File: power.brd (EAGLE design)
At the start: 95.2 x 82.5 mm, 60 parts, among them IC1 7812DT, IC2 7805TV, IC3 78L05F, U1 P82B96D, U2 P82B96D

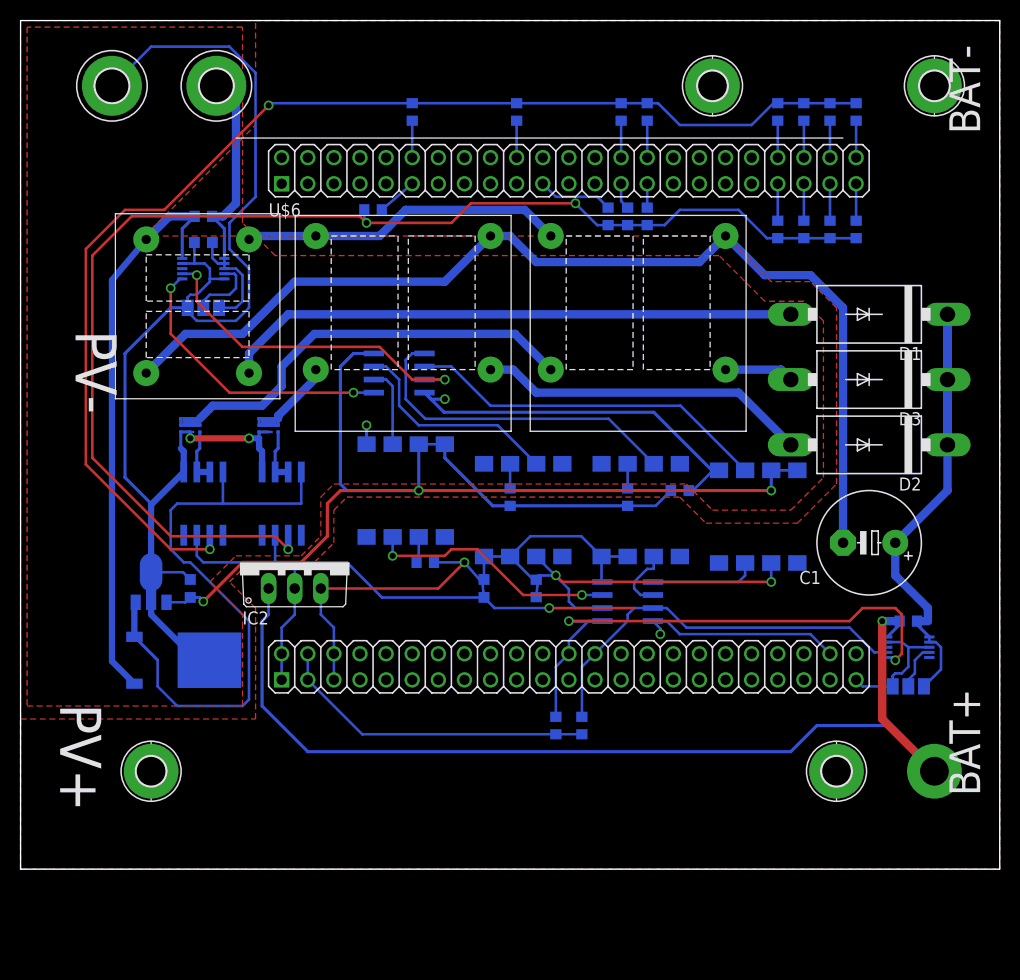
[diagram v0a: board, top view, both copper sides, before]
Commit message: sending out for another prototype
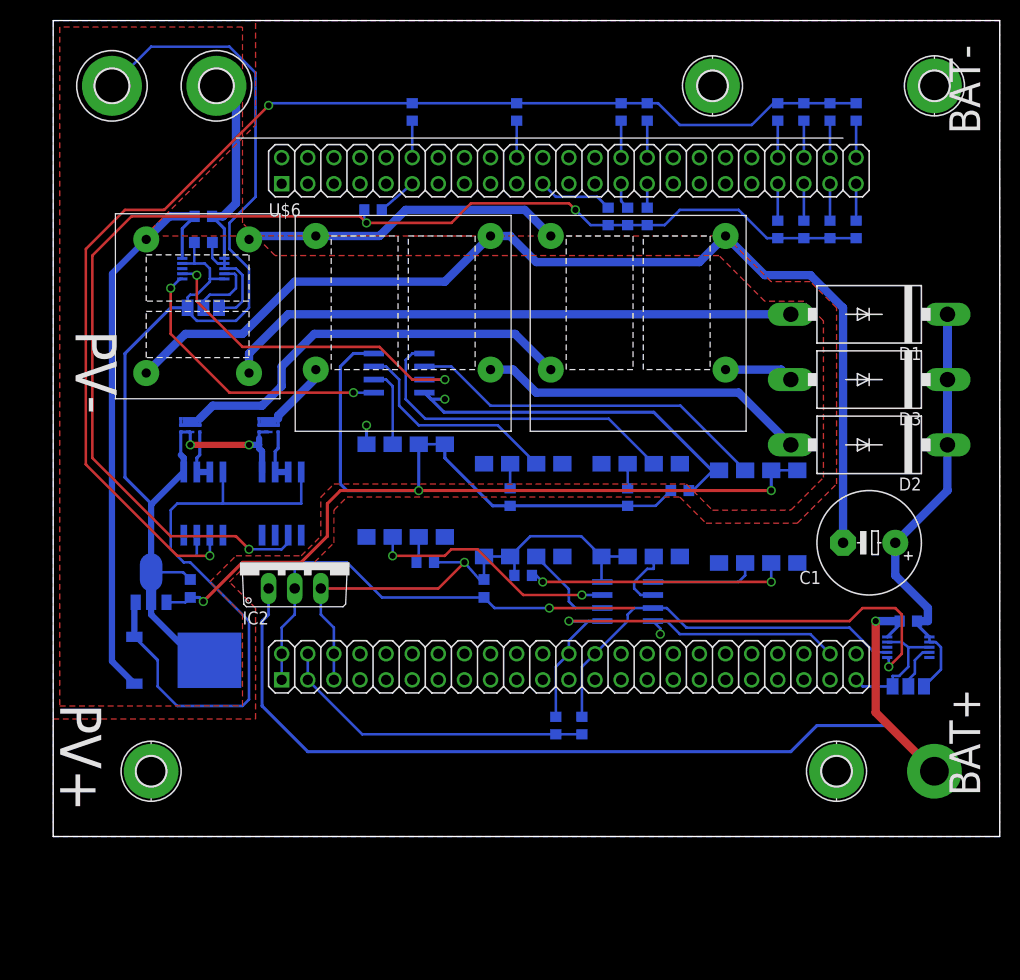
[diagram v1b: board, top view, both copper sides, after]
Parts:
- moved R5 1.80 mm to (42.5, 22.2), turned to 180 degrees
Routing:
- net GND: track 197.6 -> 183.0 mm
- net N$7: track 26.9 -> 25.4 mm
- net VCC: track 54.1 -> 52.6 mm
- net SCL: track 54.0 -> 55.0 mm
- net N$45: track 120.4 -> 121.3 mm
- net N$4: track 102.3 -> 103.2 mm
- net PGND: track 167.2 -> 167.8 mm
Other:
- board size 95.2 x 82.5 mm -> 92.1 x 79.4 mm

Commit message: fixed labels
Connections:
- removed net N$17: U$6.77
- removed net N$18: U$6.76
- removed net N$19: U$6.75
- removed net N$20: U$6.87
- removed net N$22: U$6.74
- removed net N$23: U$6.73
- removed net N$24: U$6.71

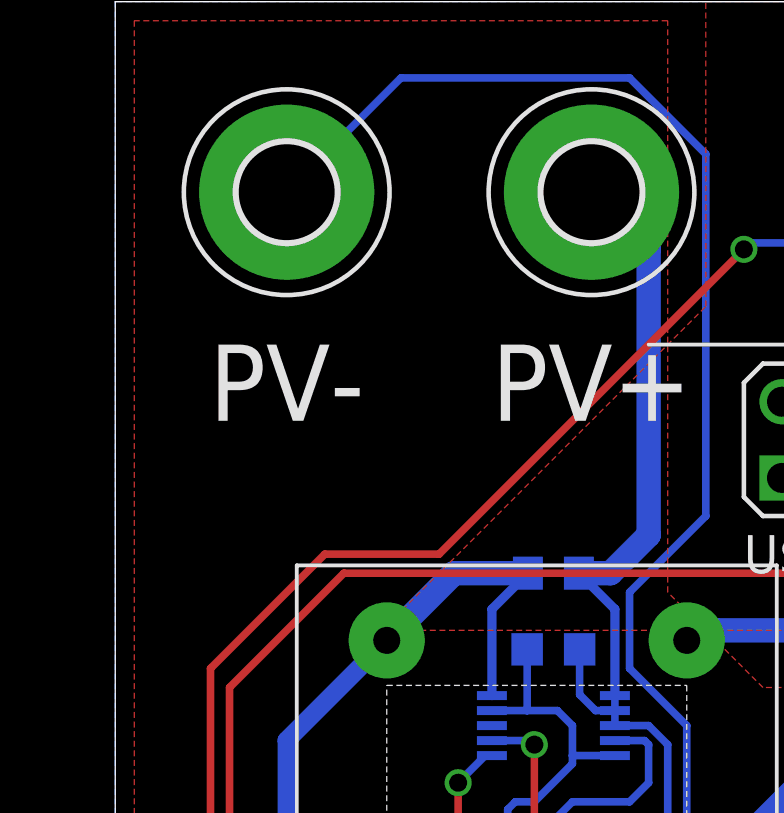
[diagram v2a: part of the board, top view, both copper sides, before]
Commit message: input capacitor? might help.
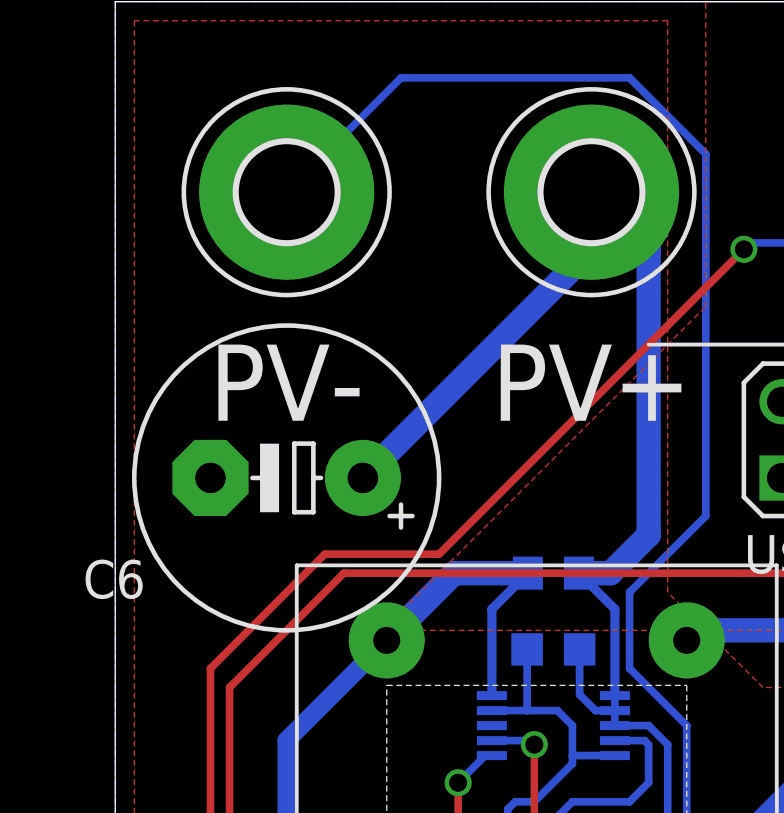
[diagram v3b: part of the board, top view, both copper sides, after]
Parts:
- added C6: 100u, rcl:E5-10,5
- C1: value (none) -> 100u
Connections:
- net PGND: now also C6.-
- net PV: now also C6.+
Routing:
- net PV: track 30.7 -> 43.3 mm
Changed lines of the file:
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@@
 <element name="D2" library="diode" package="DO201-15" value="BY500" x="76.2" y="34.925" rot="R180"/>
 <element name="D3" library="diode" package="DO201-15" value="BY500" x="76.2" y="41.275" rot="R180"/>
-<element name="C1" library="rcl" package="E5-10,5" value="" x="76.2" y="25.4" rot="R180"/>
+<element name="C1" library="rcl" package="E5-10,5" value="100u" x="76.2" y="25.4" rot="R180"/>
 <element name="R1" library="rcl" package="R0603" value="0R2" x="80.01" y="17.78" rot="MR0"/>
 <element name="R2" library="rcl" package="R0603" value="0R2" x="11.43" y="57.15" rot="MR0"/>
@@
 <element name="C4" library="rcl" package="C0603K" value="0.1u" x="57.785" y="30.48" rot="MR180"/>
 <element name="C5" library="rcl" package="C0603K" value="0.1u" x="38.735" y="20.955" rot="MR270"/>
+<element name="C6" library="rcl" package="E5-10,5" value="100u" x="2.54" y="60.325" rot="R180"/>
 </elements>
 <signals>
@@
 <wire x1="14.605" y1="58.42" x2="13.335" y2="57.15" width="0.8128" layer="16"/>
 <wire x1="13.335" y1="57.15" x2="12.28" y2="57.15" width="0.8128" layer="16"/>
+<contactref element="C6" pad="+"/>
+<wire x1="5.08" y1="60.325" x2="12.7" y2="67.945" width="0.8128" layer="16"/>
+<wire x1="12.7" y1="67.945" x2="12.7" y2="69.85" width="0.8128" layer="16"/>
 </signal>
 <signal name="N$10">
@@
 <wire x1="12.065" y1="51.07" x2="12.065" y2="50.8" width="0.254" layer="16"/>
 <wire x1="15.875" y1="34.925" x2="16.855" y2="34.925" width="0.6096" layer="16"/>
+<contactref element="C6" pad="-"/>
 </signal>
 <signal name="N$8">

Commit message: important fixes... and that 7812 that isn't actually a 7812 is still a problem
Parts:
- moved C4 33.3 mm to (25.4, 38.1)
- moved R31 6.54 mm to (49.5, 35.6), turned to 0 degrees
- moved R32 5.68 mm to (38.7, 34.9), turned to 0 degrees
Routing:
- net N$43: track 126.0 -> 105.7 mm, vias 3 -> 4
- net N$49: track 2.39 -> 3.44 mm
- net PGND: track 167.8 -> 166.8 mm
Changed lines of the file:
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@@
 <?xml version="1.0" encoding="utf-8"?>
 <!DOCTYPE eagle SYSTEM "eagle.dtd">
-<eagle version="6.5.1">
+<eagle version="6.5.0">
 <drawing>
 <settings>
@@
 <grid distance="0.025" unitdist="inch" unit="inch" style="lines" multiple="5" display="yes" altdistance="0.02" altunitdist="inch" altunit="inch"/>
 <layers>
-<layer number="1" name="Top" color="4" fill="1" visible="yes" active="yes"/>
+<layer number="1" name="Top" color="4" fill="1" visible="no" active="yes"/>
 <layer number="2" name="Route2" color="1" fill="3" visible="yes" active="yes"/>
 <layer number="3" name="Route3" color="4" fill="3" visible="yes" active="yes"/>
@@
 <element name="R5" library="rcl" package="R0603" value="560" x="42.545" y="22.225" rot="MR180"/>
 <element name="R6" library="rcl" package="R0603" value="560" x="33.02" y="23.495" rot="MR0"/>
-<element name="R31" library="rcl" package="R0603" value="560" x="52.705" y="29.845" rot="MR270"/>
-<element name="R32" library="rcl" package="R0603" value="560" x="41.275" y="29.845" rot="MR270"/>
+<element name="R31" library="rcl" package="R0603" value="560" x="49.53" y="35.56" rot="MR0"/>
+<element name="R32" library="rcl" package="R0603" value="560" x="38.735" y="34.925" rot="MR0"/>
 <element name="IC3" library="linear" package="SOT89" value="78L05F" x="6.35" y="21.59" rot="MR0"/>
 <element name="C2" library="rcl" package="C0603K" value="0.1u" x="10.16" y="20.955" rot="MR90"/>
 <element name="C3" library="rcl" package="C0603K" value="0.1u" x="11.43" y="54.61" rot="MR0"/>
-<element name="C4" library="rcl" package="C0603K" value="0.1u" x="57.785" y="30.48" rot="MR180"/>
+<element name="C4" library="rcl" package="C0603K" value="0.1u" x="25.4" y="38.1" rot="MR180"/>
 <element name="C5" library="rcl" package="C0603K" value="0.1u" x="38.735" y="20.955" rot="MR270"/>
 <element name="C6" library="rcl" package="E5-10,5" value="100u" x="2.54" y="60.325" rot="R180"/>
@@
 <wire x1="10.795" y1="46.99" x2="9.906" y2="47.879" width="0.254" layer="16"/>
 <wire x1="9.906" y1="47.879" x2="9.906" y2="48.26" width="0.254" layer="16"/>
-<wire x1="58.66" y1="30.48" x2="59.055" y2="30.48" width="0.254" layer="16"/>
-<wire x1="59.055" y1="30.48" x2="60.96" y2="32.385" width="0.254" layer="16"/>
 <wire x1="60.96" y1="32.385" x2="61.5315" y2="32.385" width="0.254" layer="16"/>
 <wire x1="61.5315" y1="32.385" x2="61.595" y2="32.4485" width="0.254" layer="16"/>
@@
 <wire x1="15.875" y1="34.925" x2="16.855" y2="34.925" width="0.6096" layer="16"/>
 <contactref element="C6" pad="-"/>
+<wire x1="26.275" y1="38.1" x2="26.9875" y2="38.1" width="0.3048" layer="16"/>
+<wire x1="26.9875" y1="38.1" x2="27.305" y2="37.7825" width="0.3048" layer="16"/>
+<wire x1="27.305" y1="37.7825" x2="27.305" y2="36.83" width="0.3048" layer="16"/>
 </signal>
 <signal name="N$8">
@@
 <contactref element="OK3" pad="P$2"/>
 <contactref element="R32" pad="1"/>
-<wire x1="41.275" y1="33.0835" x2="41.275" y2="30.695" width="0.254" layer="16"/>
+<wire x1="39.585" y1="34.925" x2="39.585" y2="34.7735" width="0.3048" layer="16"/>
+<wire x1="39.585" y1="34.7735" x2="41.275" y2="33.0835" width="0.3048" layer="16"/>
 </signal>
 <signal name="N$49">
 <contactref element="OK1" pad="P$2"/>
 <contactref element="R31" pad="1"/>
-<wire x1="52.705" y1="30.695" x2="52.705" y2="33.0835" width="0.254" layer="16"/>
+<wire x1="50.38" y1="35.56" x2="50.38" y2="35.4085" width="0.3048" layer="16"/>
+<wire x1="50.38" y1="35.4085" x2="52.705" y2="33.0835" width="0.3048" layer="16"/>
 </signal>
 <signal name="N$50">
@@
 <contactref element="U1" pad="8"/>
 <contactref element="C4" pad="1"/>
-<wire x1="52.705" y1="28.995" x2="55.425" y2="28.995" width="0.254" layer="16"/>
-<wire x1="55.425" y1="28.995" x2="56.91" y2="30.48" width="0.254" layer="16"/>
-<wire x1="52.705" y1="28.995" x2="41.275" y2="28.995" width="0.3048" layer="16"/>
 <contactref element="OK2" pad="P$8"/>
 <contactref element="OK4" pad="P$8"/>
@@
 <wire x1="66.675" y1="32.4485" x2="66.675" y2="30.48" width="0.3048" layer="16"/>
 <via x="66.675" y="30.48" extent="1-16" drill="0.6" shape="square"/>
-<wire x1="66.675" y1="30.48" x2="32.385" y2="30.48" width="0.3048" layer="1"/>
-<wire x1="32.385" y1="30.48" x2="24.765" y2="30.48" width="0.3048" layer="1"/>
+<wire x1="66.675" y1="30.48" x2="46.99" y2="30.48" width="0.3048" layer="1"/>
+<wire x1="46.99" y1="30.48" x2="32.385" y2="33.02" width="0.3048" layer="1"/>
+<wire x1="32.385" y1="33.02" x2="24.765" y2="30.48" width="0.3048" layer="1"/>
 <wire x1="24.765" y1="30.48" x2="23.495" y2="29.21" width="0.3048" layer="1"/>
 <wire x1="23.495" y1="29.21" x2="23.495" y2="26.035" width="0.3048" layer="1"/>
@@
 <wire x1="11.43" y1="19.685" x2="11.035" y2="20.08" width="0.3048" layer="16"/>
 <wire x1="11.035" y1="20.08" x2="10.16" y2="20.08" width="0.3048" layer="16"/>
-<wire x1="32.385" y1="34.9885" x2="32.385" y2="30.48" width="0.3048" layer="16"/>
-<via x="32.385" y="30.48" extent="1-16" drill="0.6" shape="square"/>
-<wire x1="34.925" y1="34.9885" x2="34.925" y2="33.655" width="0.3048" layer="16"/>
-<wire x1="34.925" y1="33.655" x2="39.585" y2="28.995" width="0.3048" layer="16"/>
-<wire x1="39.585" y1="28.995" x2="41.275" y2="28.995" width="0.3048" layer="16"/>
+<wire x1="32.385" y1="34.9885" x2="32.385" y2="33.02" width="0.3048" layer="16"/>
+<via x="32.385" y="33.02" extent="1-16" drill="0.6" shape="square"/>
 <wire x1="28.0162" y1="43.815" x2="26.035" y2="43.815" width="0.3048" layer="16"/>
 <wire x1="26.035" y1="43.815" x2="24.765" y2="42.545" width="0.3048" layer="16"/>
-<wire x1="24.765" y1="42.545" x2="24.765" y2="31.115" width="0.3048" layer="16"/>
-<wire x1="24.765" y1="31.115" x2="25.4" y2="30.48" width="0.3048" layer="16"/>
-<wire x1="25.4" y1="30.48" x2="32.385" y2="30.48" width="0.3048" layer="16"/>
+<wire x1="24.765" y1="42.545" x2="24.765" y2="38.1" width="0.3048" layer="16"/>
+<wire x1="24.765" y1="38.1" x2="24.765" y2="33.655" width="0.3048" layer="16"/>
+<wire x1="24.765" y1="33.655" x2="25.4" y2="33.02" width="0.3048" layer="16"/>
+<wire x1="25.4" y1="33.02" x2="32.385" y2="33.02" width="0.3048" layer="16"/>
+<wire x1="24.525" y1="38.1" x2="24.765" y2="38.1" width="0.3048" layer="16"/>
+<wire x1="34.925" y1="34.9885" x2="37.8215" y2="34.9885" width="0.3048" layer="16"/>
+<wire x1="37.8215" y1="34.9885" x2="37.885" y2="34.925" width="0.3048" layer="16"/>
+<wire x1="48.68" y1="35.56" x2="46.99" y2="35.56" width="0.3048" layer="16"/>
+<via x="46.99" y="35.56" extent="1-16" drill="0.6" shape="square"/>
+<wire x1="46.99" y1="35.56" x2="46.99" y2="30.48" width="0.3048" layer="1"/>
 </signal>
 <signal name="N$46">
